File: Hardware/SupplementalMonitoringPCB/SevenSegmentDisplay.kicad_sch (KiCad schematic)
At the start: 9 parts, among them U7 INND-SS30RAB

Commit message: schm actually done now whoops
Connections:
- net a: no longer R9.2
- net b: no longer R10.2
- net c: no longer R5.1
- net d: no longer R4.1
- net e: no longer R3.1
- net f: no longer R8.2
- net g: no longer R7.2
- net h: no longer R6.1
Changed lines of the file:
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@@
 	(wire
 		(pts
-			(xy 168.91 93.98) (xy 172.72 93.98)
+			(xy 157.48 88.9) (xy 180.34 88.9)
 		)
 		(stroke
@@
 	(wire
 		(pts
-			(xy 168.91 91.44) (xy 172.72 91.44)
-		)
-		(stroke
-			(width 0)
-			(type default)
-		)
-	)
-	(wire
-		(pts
 			(xy 113.03 91.44) (xy 116.84 91.44)
 		)
@@
 		(pts
 			(xy 157.48 86.36) (xy 161.29 86.36)
-		)
-		(stroke
-			(width 0)
-			(type default)
-		)
-	)
-	(wire
-		(pts
-			(xy 102.87 93.98) (xy 105.41 93.98)
 		)
 		(stroke
@@
 	(wire
 		(pts
-			(xy 102.87 83.82) (xy 105.41 83.82)
-		)
-		(stroke
-			(width 0)
-			(type default)
-		)
-	)
-	(wire
-		(pts
-			(xy 168.91 83.82) (xy 172.72 83.82)
-		)
-		(stroke
-			(width 0)
-			(type default)
-		)
-	)
-	(wire
-		(pts
 			(xy 95.25 86.36) (xy 95.25 88.9)
-		)
-		(stroke
-			(width 0)
-			(type default)
-		)
-	)
-	(wire
-		(pts
-			(xy 168.91 86.36) (xy 172.72 86.36)
-		)
-		(stroke
-			(width 0)
-			(type default)
-		)
-	)
-	(wire
-		(pts
-			(xy 102.87 86.36) (xy 105.41 86.36)
 		)
 		(stroke
@@
 		)
 		(stroke
-			(width 0)
-			(type default)
-		)
-	)
-	(wire
-		(pts
-			(xy 102.87 91.44) (xy 105.41 91.44)
-		)
-		(stroke
-			(width 0)
-			(type default)
-		)
-	)
-	(wire
-		(pts
-			(xy 180.34 88.9) (xy 157.48 88.9)
-		)
-		(stroke

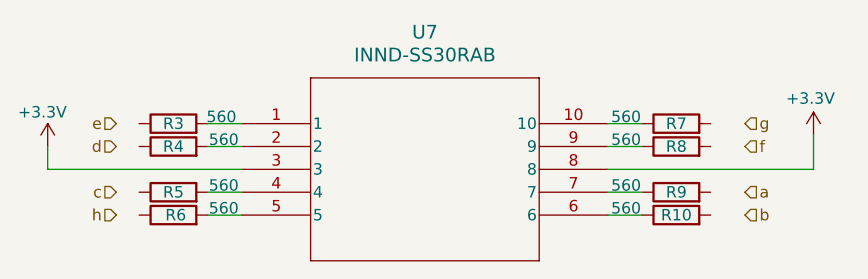
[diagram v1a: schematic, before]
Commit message: add pullup for SRCLR
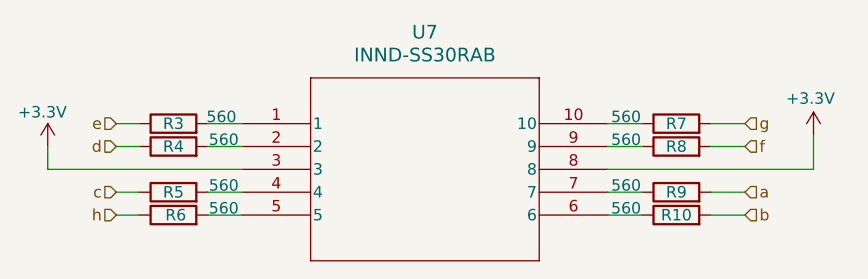
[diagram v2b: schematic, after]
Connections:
- net a: now also R9.2
- net b: now also R10.2
- net c: now also R5.1
- net d: now also R4.1
- net e: now also R3.1
- net f: now also R8.2
- net g: now also R7.2
- net h: now also R6.1
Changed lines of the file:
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@@
+	(wire
+		(pts
+			(xy 102.87 91.44) (xy 105.41 91.44)
+		)
+		(stroke
+			(width 0)
+			(type default)
+		)
+	)
 	(wire
 		(pts
@@
 	(wire
 		(pts
+			(xy 102.87 93.98) (xy 105.41 93.98)
+		)
+		(stroke
+			(width 0)
+			(type default)
+		)
+	)
+	(wire
+		(pts
 			(xy 157.48 86.36) (xy 161.29 86.36)
+		)
+		(stroke
+			(width 0)
+			(type default)
+		)
+	)
+	(wire
+		(pts
+			(xy 102.87 83.82) (xy 105.41 83.82)
 		)
 		(stroke
@@
 	(wire
 		(pts
+			(xy 168.91 83.82) (xy 172.72 83.82)
+		)
+		(stroke
+			(width 0)
+			(type default)
+		)
+	)
+	(wire
+		(pts
 			(xy 157.48 93.98) (xy 161.29 93.98)
+		)
+		(stroke
+			(width 0)
+			(type default)
+		)
+	)
+	(wire
+		(pts
+			(xy 168.91 86.36) (xy 172.72 86.36)
 		)
 		(stroke
@@
 		)
 		(stroke
+			(width 0)
+			(type default)
+		)
+	)
+	(wire
+		(pts
+			(xy 168.91 93.98) (xy 172.72 93.98)
+		)
+		(stroke
+			(width 0)
+			(type default)
+		)
+	)
+	(wire
+		(pts
+			(xy 168.91 91.44) (xy 172.72 91.44)
+		)
+		(stroke
+			(width 0)
+			(type default)
+		)
+	)
+	(wire
+		(pts
+			(xy 102.87 86.36) (xy 105.41 86.36)
+		)
+		(stroke

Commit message: seven segment routing
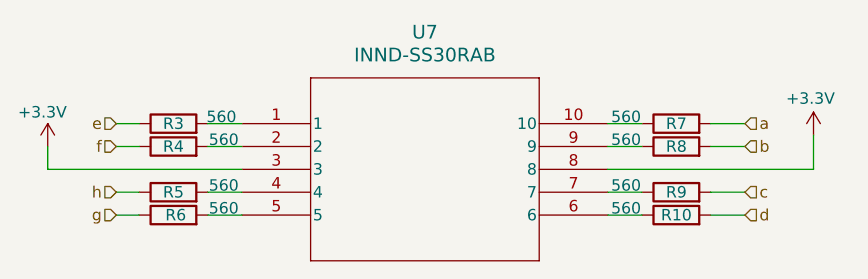
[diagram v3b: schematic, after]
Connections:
- net a: now also R7.2; no longer R9.2
- net b: now also R8.2; no longer R10.2
- net c: now also R9.2; no longer R5.1
- net d: now also R10.2; no longer R4.1
- net f: now also R4.1; no longer R8.2
- net g: now also R6.1; no longer R7.2
- net h: now also R5.1; no longer R6.1
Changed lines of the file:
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@@
+	(wire
+		(pts
+			(xy 95.25 88.9) (xy 116.84 88.9)
+		)
+		(stroke
+			(width 0)
+			(type default)
+		)
+	)
+	(wire
+		(pts
+			(xy 168.91 86.36) (xy 172.72 86.36)
+		)
+		(stroke
+			(width 0)
+			(type default)
+		)
+	)
+	(wire
+		(pts
+			(xy 157.48 83.82) (xy 161.29 83.82)
+		)
+		(stroke
+			(width 0)
+			(type default)
+		)
+	)
+	(wire
+		(pts
+			(xy 168.91 83.82) (xy 172.72 83.82)
+		)
+		(stroke
+			(width 0)
+			(type default)
+		)
+	)
+	(wire
+		(pts
+			(xy 157.48 88.9) (xy 180.34 88.9)
+		)
+		(stroke
+			(width 0)
+			(type default)
+		)
+	)
+	(wire
+		(pts
+			(xy 180.34 85.09) (xy 180.34 88.9)
+		)
+		(stroke
+			(width 0)
+			(type default)
+		)
+	)
+	(wire
+		(pts
+			(xy 157.48 91.44) (xy 161.29 91.44)
+		)
+		(stroke
+			(width 0)
+			(type default)
+		)
+	)
+	(wire
+		(pts
+			(xy 168.91 93.98) (xy 172.72 93.98)
+		)
+		(stroke
+			(width 0)
+			(type default)
+		)
+	)
+	(wire
+		(pts
+			(xy 102.87 86.36) (xy 105.41 86.36)
+		)
+		(stroke
+			(width 0)
+			(type default)
+		)
+	)
+	(wire
+		(pts
+			(xy 113.03 91.44) (xy 116.84 91.44)
+		)
+		(stroke
+			(width 0)
+			(type default)
+		)
+	)
+	(wire
+		(pts
+			(xy 157.48 86.36) (xy 161.29 86.36)
+		)
+		(stroke
+			(width 0)
+			(type default)
+		)
+	)
 	(wire
 		(pts
@@
 	(wire
 		(pts
-			(xy 95.25 88.9) (xy 116.84 88.9)
-		)
-		(stroke
-			(width 0)
-			(type default)
-		)
-	)
-	(wire
-		(pts
-			(xy 157.48 83.82) (xy 161.29 83.82)
-		)
-		(stroke
-			(width 0)
-			(type default)
-		)
-	)
-	(wire
-		(pts
-			(xy 157.48 88.9) (xy 180.34 88.9)
-		)
-		(stroke
-			(width 0)
-			(type default)
-		)
-	)
-	(wire
-		(pts
-			(xy 180.34 85.09) (xy 180.34 88.9)
-		)
-		(stroke
-			(width 0)
-			(type default)
-		)
-	)
-	(wire
-		(pts
-			(xy 157.48 91.44) (xy 161.29 91.44)
-		)
-		(stroke
-			(width 0)
-			(type default)
-		)
-	)
-	(wire
-		(pts
-			(xy 113.03 91.44) (xy 116.84 91.44)
+			(xy 113.03 86.36) (xy 116.84 86.36)
+		)
+		(stroke
+			(width 0)
+			(type default)
+		)
+	)
+	(wire
+		(pts
+			(xy 157.48 93.98) (xy 161.29 93.98)
+		)
+		(stroke
+			(width 0)
+			(type default)
+		)
+	)
+	(wire
+		(pts
+			(xy 102.87 83.82) (xy 105.41 83.82)
 		)
 		(stroke
@@
 	(wire
 		(pts
-			(xy 157.48 86.36) (xy 161.29 86.36)
-		)
-		(stroke
-			(width 0)
-			(type default)
-		)
-	)
-	(wire
-		(pts
-			(xy 102.87 83.82) (xy 105.41 83.82)
-		)
-		(stroke
-			(width 0)
-			(type default)
-		)
-	)
-	(wire
-		(pts
-			(xy 113.03 86.36) (xy 116.84 86.36)
-		)
-		(stroke
-			(width 0)
-			(type default)
-		)
-	)
-	(wire
-		(pts
-			(xy 168.91 83.82) (xy 172.72 83.82)
-		)
-		(stroke
-			(width 0)
-			(type default)
-		)
-	)
-	(wire
-		(pts
-			(xy 157.48 93.98) (xy 161.29 93.98)
-		)
-		(stroke
-			(width 0)
-			(type default)
-		)
-	)
-	(wire
-		(pts
-			(xy 168.91 86.36) (xy 172.72 86.36)
-		)
-		(stroke
-			(width 0)
-			(type default)
-		)
-	)
-	(wire
-		(pts
 			(xy 95.25 86.36) (xy 95.25 88.9)
 		)
@@
 	(wire
 		(pts
-			(xy 168.91 93.98) (xy 172.72 93.98)
+			(xy 113.03 93.98) (xy 116.84 93.98)
 		)
 		(stroke
@@
 	(wire
 		(pts
-			(xy 102.87 86.36) (xy 105.41 86.36)
-		)
-		(stroke
-			(width 0)
-			(type default)
-		)
-	)
-	(wire
-		(pts
-			(xy 113.03 93.98) (xy 116.84 93.98)
-		)
-		(stroke
-			(width 0)
-			(type default)
-		)
-	)
-	(wire
-		(pts
 			(xy 113.03 83.82) (xy 116.84 83.82)
 		)
@@
 	(hierarchical_label "h"
 		(shape input)
+		(at 102.87 91.44 180)
+		(effects
+			(font
+				(size 1.27 1.27)
+			)
+			(justify right)
+		)
+	)
+	(hierarchical_label "d"
+		(shape input)
+		(at 172.72 93.98 0)
+		(effects
+			(font
+				(size 1.27 1.27)
+			)
+			(justify left)
+		)
+	)
+	(hierarchical_label "a"
+		(shape input)
+		(at 172.72 83.82 0)
+		(effects
+			(font
+				(size 1.27 1.27)
+			)
+			(justify left)
+		)
+	)
+	(hierarchical_label "c"
+		(shape input)
+		(at 172.72 91.44 0)
+		(effects
+			(font
+				(size 1.27 1.27)
+			)
+			(justify left)
+		)
+	)
+	(hierarchical_label "b"
+		(shape input)
+		(at 172.72 86.36 0)
+		(effects
+			(font
+				(size 1.27 1.27)
+			)
+			(justify left)
+		)
+	)
+	(hierarchical_label "f"
+		(shape input)
+		(at 102.87 86.36 180)
+		(effects
+			(font
+				(size 1.27 1.27)
+			)
+			(justify right)
+		)
+	)
+	(hierarchical_label "g"
+		(shape input)
 		(at 102.87 93.98 180)
 		(effects
@@
 		)
 	)
-	(hierarchical_label "d"
-		(shape input)
-		(at 102.87 86.36 180)
-		(effects
-			(font
-				(size 1.27 1.27)
-			)
-			(justify right)
-		)
-	)
-	(hierarchical_label "a"
-		(shape input)
-		(at 172.72 91.44 0)
-		(effects
-			(font
-				(size 1.27 1.27)
-			)
-			(justify left)
-		)
-	)
-	(hierarchical_label "c"
-		(shape input)
-		(at 102.87 91.44 180)
-		(effects
-			(font
-				(size 1.27 1.27)
-			)
-			(justify right)
-		)
-	)
-	(hierarchical_label "b"
-		(shape input)
-		(at 172.72 93.98 0)
-		(effects
-			(font
-				(size 1.27 1.27)
-			)
-			(justify left)
-		)
-	)
-	(hierarchical_label "f"
-		(shape input)
-		(at 172.72 86.36 0)
-		(effects
-			(font
-				(size 1.27 1.27)
-			)
-			(justify left)
-		)
-	)
-	(hierarchical_label "g"
-		(shape input)
-		(at 172.72 83.82 0)
-		(effects
-			(font
-				(size 1.27 1.27)
-			)
-			(justify left)
-		)
-	)

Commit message: routing mostly done
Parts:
- R10, R3, R4, R5, R6, R7, R8, R9: value 560 -> 470; LCSC P/N (none) -> C23179; P/N (none) -> CRCW1206470RFKEA

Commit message: board done and in cart
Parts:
- U7: P/N (none) -> INND-SS30RAB
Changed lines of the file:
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@@
 			)
 		)
-		(property "Description" ""
+		(property "Description" "SMD Single Digit Display"
 			(at 116.84 83.82 0)
 			(effects
@@
 			(at 116.84 83.82 0)
 			(effects
+				(font
+					(size 1.27 1.27)
+				)
+				(hide yes)
+			)
+		)
+		(property "P/N" "INND-SS30RAB "
+			(at 116.84 83.82 0)
+			(effects
